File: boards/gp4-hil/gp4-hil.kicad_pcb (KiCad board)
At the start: 4 copper layers, 160 x 62 mm, 452 parts, among them J1 BEL_FUSE_0826-1G1T-23-F, J2 XILINX_JTAG, J3 XILINX_JTAG_ICESIDE, J4 XILINX_JTAG_ICESIDE, K1 CONN_3_PWROUT, P1 GPAK_ZIF, P2 2x10 HEADER, Q1 SSM6N58NU, Q11 SSM6N58NU, Q12 DMP2069UFY4, Q13 SSM6N58NU, Q14 SSM6N58NU, Q15 SSM6N58NU, Q16 SSM6N58NU, Q17 SSM6N58NU, Q18 SSM6N58NU, Q19 SSM6N58NU, Q20 SSM6N58NU, Q21 SSM6N58NU, Q22 DMP2069UFY4, U1 MIC2288-DFN, U10 AD9609, U11 DAC084S085, U12 DAC084S085, U13 DAC084S085, U14 DAC084S085, U15 TS3A4751, U16 TS3A4751, U17 TS3A4751, U18 TS3A4751, U19 TS3A4751, U2 XC7A100T-1FTG256C, U20 SIP32408, U21 SIP32408, U22 SIP32408, U23 SIP32408, U24 SIP32408, U25 TS3A4751, U26 TS3A4751, U27 TS3A4751, U28 TS3A4751, U29 TXB0104RUT, U3 LTC3374-QFN, U30 TXB0104RUT, U31 ADA4937-2, U32 SIP32408, U33 125 MHz, U34 INA199A2RSW, U35 INA199A2RSW, U36 INA199A2RSW, U4 SIP32408, U5 KSZ9031RN, U6 W25Q32FW, U7 25 MHz, U8 ADG726, U9 AD9609

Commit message: Continued work on GreenPak test board
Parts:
- C146, C148, C150, C153, C154, C185, C42, C43, C44, C45, R139, R141, R17, R22: moved to B.Cu
- moved C154 101.3 mm to (123.0, 70.6), turned to 180 degrees
- moved C152 96.3 mm to (116.7, 83.5), turned to 90 degrees
- moved R141 93.9 mm to (124.7, 71.0), turned to 90 degrees
- moved R74 89.9 mm to (127.5, 77.4), turned to 180 degrees
- moved R140 88.3 mm to (116.2, 85.0)
- moved C159 86.5 mm to (60.2, 51.5)
- moved C160 86.5 mm to (63.4, 48.5)
- moved C161 86.5 mm to (60.0, 48.5)
- moved C162 86.5 mm to (63.5, 51.3)
- moved U19 86.5 mm to (56.3, 50.9)
- moved U25 86.5 mm to (46.2, 50.5)
- moved U26 86.5 mm to (51.6, 51.1)
- moved U27 86.5 mm to (41.2, 50.6)
- moved U28 86.5 mm to (35.8, 51.0)
- moved C153 85.3 mm to (123.0, 71.4), turned to 180 degrees
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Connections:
- C151 pad 1: Net-(C151-Pad1) -> /Analog IO/ADC_B_CLKX_P
- C152 pad 1: Net-(C152-Pad1) -> /Analog IO/ADC_B_CLKX_N
- C153 pad 1: Net-(C153-Pad1) -> /Analog IO/ADC_A_CLKX_P
- C154 pad 1: Net-(C154-Pad1) -> /Analog IO/ADC_A_CLKX_N
- R140 pad 1: Net-(C151-Pad1) -> /Analog IO/ADC_B_CLKX_P
- R140 pad 2: Net-(C152-Pad1) -> /Analog IO/ADC_B_CLKX_N
- R141 pad 1: Net-(C153-Pad1) -> /Analog IO/ADC_A_CLKX_P
- R141 pad 2: Net-(C154-Pad1) -> /Analog IO/ADC_A_CLKX_N
- U2 pad A12: /Analog IO/ADC_B_D2 -> /Analog IO/ADC_B_MODE
- U2 pad A13: Net-(C151-Pad1) -> /Analog IO/ADC_SCLK
- U2 pad A14: Net-(C152-Pad1) -> /Analog IO/ADC_B_SDIO
- U2 pad A15: /Analog IO/ADC_CS_N -> /Analog IO/ADC_B_D5
- U2 pad A8: /Analog IO/MUX_A3 -> /Analog IO/ADC_B_CLKX_P
- U2 pad A9: /Analog IO/MUX_CS_A_N -> /Analog IO/ADC_B_CLKX_N
- U2 pad B11: /Analog IO/ADC_B_D0 -> /Analog IO/MUX_A3
- U2 pad B12: /Analog IO/ADC_B_D1 -> /Analog IO/ADC_CS_N
- U2 pad B14: /Analog IO/ADC_B_D8 -> /Analog IO/ADC_B_D6
- U2 pad B15: /Analog IO/ADC_B_D9 -> /Analog IO/ADC_B_D2
- U2 pad B16: Net-(C154-Pad1) -> /Analog IO/ADC_B_D4
- U2 pad C11: /Analog IO/ADC_SCLK -> /Analog IO/DAC_SYNC_N
- U2 pad C12: /Analog IO/ADC_B_SDIO -> /Analog IO/ADC_A_MODE
- U2 pad C13: (no net) -> /Analog IO/ADC_A_SDIO
- U2 pad C14: /Analog IO/ADC_B_D7 -> /Analog IO/ADC_B_D8
- U2 pad C16: Net-(C153-Pad1) -> /Analog IO/ADC_B_D3
- U2 pad D14: /Analog IO/DAC_SCLK -> /Analog IO/ADC_A_CLKX_P
- U2 pad D15: /Analog IO/DAC_SYNC_N -> /Analog IO/ADC_A_CLKX_N
- U2 pad D16: /Analog IO/ADC_B_D6 -> /Analog IO/ADC_B_D1
- U2 pad D8: /Analog IO/ADC_B_D3 -> /Analog IO/DAC_SCLK
- U2 pad D9: /Analog IO/ADC_B_D4 -> /Analog IO/DAC_C_DIN
- U2 pad E15: /Analog IO/ADC_B_D5 -> /Analog IO/ADC_B_D0
- U2 pad F13: /Analog IO/ADC_B_MODE -> /Analog IO/ADC_B_D9
- U2 pad G11: /Analog IO/ADC_A_MODE -> /Analog IO/MUX_CS_A_N
- U2 pad G12: /Analog IO/ADC_A_D8 -> /Analog IO/ADC_B_D7
- U2 pad H11: /Analog IO/DAC_C_DIN -> (no net)
- U2 pad H12: /Analog IO/ADC_A_SDIO -> /Analog IO/ADC_A_D8
- U8 pad 30: /Analog IO/ADC_GPIO20 -> /Analog IO/ADC_VDD2
- U8 pad 32: /Analog IO/ADC_VDD2 -> /Analog IO/ADC_GPIO20
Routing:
- net /Analog IO/A1V8: track 17.3 -> 102.0 mm, vias 5 -> 13
- net /Analog IO/GND: track 1086.6 -> 1147.2 mm, vias 210 -> 222
- net /Analog IO/ADC_GPIO20: track 0.00 -> 54.0 mm, vias 0 -> 1
- net /Analog IO/ADC_A_MODE: track 2.04 -> 37.8 mm, vias 1 -> 4
- net /Analog IO/ADC_A_CLKX_P: track 0.00 -> 35.0 mm, vias 0 -> 1
- net /Analog IO/ADC_A_CLKX_N: track 0.00 -> 34.9 mm, vias 0 -> 1
- net /Analog IO/ADC_A_DCLK: track 9.65 -> 42.7 mm
- net /Analog IO/ADC_CS_N: track 0.00 -> 31.1 mm, vias 0 -> 2
- net /Analog IO/ADC_B_D7: track 0.71 -> 31.3 mm, vias 1 -> 2
- net /Analog IO/ADC_A_SDIO: track 0.71 -> 31.2 mm, vias 1 -> 4
- net /Analog IO/ADC_SCLK: track 0.71 -> 28.9 mm, vias 1 -> 2
- net /Analog IO/ADC_B_D6: track 0.00 -> 27.2 mm, vias 0 -> 2
- net /Analog IO/ADC_B_D9: track 0.00 -> 26.8 mm, vias 0 -> 2
- net /Analog IO/ADC_B_D8: track 0.00 -> 25.7 mm, vias 0 -> 2
- net /Analog IO/ADC_B_D5: track 0.71 -> 25.8 mm, vias 1 -> 2
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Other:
- rule via_min_size: 0.55 -> 0.5
- board text added: "GreenPak Toolchain Test v0.1 A. Zonenberg / 2016-06-07"
- board text removed: "GreenPak Toolchain Test v0.1 A. Zonenberg / 2016-06-03"

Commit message: Added logic to check if the node displaced by a swap is legal in the current site. Fixes #9.
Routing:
- net /FPGA support/1V0: track 130.4 -> 132.2 mm
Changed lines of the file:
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@@
     (thickness 1.6)
     (drawings 64)
-    (tracks 5589)
+    (tracks 5595)
     (zones 0)
     (modules 452)
@@
   (segment (start 108 91) (end 107.5 90.5) (width 0.15) (layer F.Cu) (net 14) (status 10))
   (via (at 107.5 90.5) (size 0.55) (drill 0.3) (layers F.Cu B.Cu) (net 14))
+  (segment (start 112.900001 82.374999) (end 120.65 82.374999) (width 0.15) (layer In2.Cu) (net 15))
+  (segment (start 121.082008 79.117992) (end 120.553092 79.646908) (width 0.15) (layer In2.Cu) (net 15))
+  (segment (start 120.553092 79.646908) (end 120.553092 80.56417) (width 0.15) (layer In2.Cu) (net 15))
+  (segment (start 120.775001 82.249998) (end 120.65 82.374999) (width 0.15) (layer In2.Cu) (net 15))
+  (segment (start 120.553092 80.56417) (end 120.775001 80.786079) (width 0.15) (layer In2.Cu) (net 15))
+  (segment (start 120.775001 80.786079) (end 120.775001 82.249998) (width 0.15) (layer In2.Cu) (net 15))
+  (segment (start 124.05 79.117992) (end 126.374999 76.792993) (width 0.15) (layer In2.Cu) (net 15))
+  (segment (start 124.05 79.117992) (end 121.082008 79.117992) (width 0.15) (layer In2.Cu) (net 15))
   (segment (start 112.475 82.8) (end 112.475 77.25) (width 0.15) (layer In2.Cu) (net 15))
+  (segment (start 112.525 77.3) (end 112.475 77.25) (width 0.15) (layer In2.Cu) (net 15))
+  (segment (start 113.5 77.3) (end 112.525 77.3) (width 0.15) (layer In2.Cu) (net 15))
   (segment (start 112.475 83.75) (end 112.475 82.8) (width 0.15) (layer In2.Cu) (net 15))
   (segment (start 126.374999 75.225001) (end 126.85 74.75) (width 0.15) (layer In2.Cu) (net 15))
   (segment (start 126.85 74.75) (end 132.303002 74.75) (width 0.15) (layer In2.Cu) (net 15))
   (segment (start 112.475 82.8) (end 112.900001 82.374999) (width 0.15) (layer In2.Cu) (net 15))
-  (segment (start 112.900001 82.374999) (end 120.792993 82.374999) (width 0.15) (layer In2.Cu) (net 15))
-  (segment (start 120.792993 82.374999) (end 126.374999 76.792993) (width 0.15) (layer In2.Cu) (net 15))
   (segment (start 126.374999 76.792993) (end 126.374999 75.225001) (width 0.15) (layer In2.Cu) (net 15))
   (segment (start 115.2 78.05) (end 113.5 78.05) (width 0.15) (layer In2.Cu) (net 15))
@@
   (segment (start 113.48507 78.78507) (end 113.5 78.8) (width 0.15) (layer F.Cu) (net 15))
   (via (at 113.5 78.8) (size 0.55) (drill 0.3) (layers F.Cu B.Cu) (net 15))
-  (segment (start 113.5 77.3) (end 112.525 77.3) (width 0.15) (layer In2.Cu) (net 15))
-  (segment (start 112.525 77.3) (end 112.475 77.25) (width 0.15) (layer In2.Cu) (net 15))
   (segment (start 113.48507 78.05) (end 113.48507 77.31493) (width 0.15) (layer F.Cu) (net 15))
   (segment (start 113.48507 77.31493) (end 113.5 77.3) (width 0.15) (layer F.Cu) (net 15))

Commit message: Pushing current state of greenpak test board
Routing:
- net /FPGA support/1V0: track 132.2 -> 126.4 mm
- net /Analog IO/2V5: track 224.2 -> 228.3 mm, vias 23 -> 25
- added copper zone on F.Cu, net /Analog IO/2V5
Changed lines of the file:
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@@
   (general
     (links 1341)
-    (no_connects 444)
+    (no_connects 443)
     (area 15.966071 41.4125 184.744643 140.2125)
     (thickness 1.6)
     (drawings 64)
-    (tracks 5595)
+    (tracks 5600)
     (zones 0)
     (modules 452)
@@
   (via (at 150.4 72.3) (size 0.55) (drill 0.3) (layers F.Cu B.Cu) (net 2))
   (via (at 150.4 71.3) (size 0.55) (drill 0.3) (layers F.Cu B.Cu) (net 2))
+  (segment (start 125.1 67.4) (end 125.1 66.15) (width 0.15) (layer In2.Cu) (net 3))
+  (segment (start 125.1 66.15) (end 124.6 65.65) (width 0.15) (layer In2.Cu) (net 3))
+  (segment (start 125.1 67.4) (end 124.25 67.4) (width 0.15) (layer In2.Cu) (net 3))
+  (segment (start 124.65 68.188908) (end 124.65 67.85) (width 0.15) (layer F.Cu) (net 3))
+  (segment (start 124.65 67.85) (end 125.1 67.4) (width 0.15) (layer F.Cu) (net 3))
+  (via (at 125.1 67.4) (size 0.55) (drill 0.3) (layers F.Cu B.Cu) (net 3))
+  (segment (start 124.078859 78.386131) (end 124.078859 74.971141) (width 0.15) (layer B.Cu) (net 3))
+  (segment (start 124.078859 74.971141) (end 124.1 74.95) (width 0.15) (layer B.Cu) (net 3))
+  (segment (start 124.65 68.188908) (end 124.65 74.4) (width 0.15) (layer F.Cu) (net 3))
+  (segment (start 124.65 74.4) (end 124.1 74.95) (width 0.15) (layer F.Cu) (net 3))
+  (via (at 124.1 74.95) (size 0.55) (drill 0.3) (layers F.Cu B.Cu) (net 3))
+  (segment (start 124.25 67.4) (end 124.25 67.788908) (width 0.15) (layer F.Cu) (net 3))
+  (segment (start 124.25 67.788908) (end 124.65 68.188908) (width 0.15) (layer F.Cu) (net 3))
   (segment (start 121.525 90.1) (end 121.525 89.525) (width 0.15) (layer B.Cu) (net 3))
   (segment (start 121.525 89.525) (end 121.5 89.5) (width 0.15) (layer B.Cu) (net 3))
@@
   (segment (start 119.975001 92.225001) (end 120 92.25) (width 0.125) (layer In2.Cu) (net 3))
   (segment (start 120 92.25) (end 120 93.5) (width 0.125) (layer In2.Cu) (net 3))
-  (segment (start 124.078859 78.386131) (end 124.078859 67.571141) (width 0.15) (layer In2.Cu) (net 3))
-  (segment (start 124.078859 67.571141) (end 124.25 67.4) (width 0.15) (layer In2.Cu) (net 3))
   (segment (start 142.25 78.5) (end 129.75 78.5) (width 0.15) (layer In2.Cu) (net 3))
   (segment (start 129.75 78.5) (end 121.5 86.75) (width 0.15) (layer In2.Cu) (net 3))
@@
   (segment (start 155.22 91.405) (end 155.22 90.22) (width 0.15) (layer B.Cu) (net 10) (status 30))
   (segment (start 155.22 90.22) (end 155.2 90.2) (width 0.15) (layer B.Cu) (net 10) (status 30))
-  (segment (start 120.524999 69.971999) (end 119.1 71.396998) (width 0.15) (layer In2.Cu) (net 11))
-  (segment (start 119.1 71.396998) (end 119.128687 71.425685) (width 0.15) (layer In2.Cu) (net 11))
-  (segment (start 119.128687 71.425685) (end 119.128687 75.462845) (width 0.15) (layer In2.Cu) (net 11))
-  (segment (start 120.25 68.95) (end 120.524999 69.224999) (width 0.15) (layer In2.Cu) (net 11))
-  (segment (start 120.524999 69.224999) (end 120.524999 69.971999) (width 0.15) (layer In2.Cu) (net 11))
+  (segment (start 119.128687 75.462845) (end 119.128687 71.368311) (width 0.15) (layer In2.Cu) (net 11))
+  (segment (start 119.128687 71.368311) (end 120.524999 69.971999) (width 0.15) (layer In2.Cu) (net 11))
+  (segment (start 120.524999 69.971999) (end 120.524999 69.224999) (width 0.15) (layer In2.Cu) (net 11))
+  (segment (start 120.524999 69.224999) (end 120.25 68.95) (width 0.15) (layer In2.Cu) (net 11))
   (segment (start 87.174999 65.975001) (end 92.125001 61.024999) (width 0.15) (layer In2.Cu) (net 11))
   (segment (start 118.746998 62.8) (end 118.861092 62.8) (width 0.15) (layer In2.Cu) (net 11))
@@
   (segment (start 108 91) (end 107.5 90.5) (width 0.15) (layer F.Cu) (net 14) (status 10))
   (via (at 107.5 90.5) (size 0.55) (drill 0.3) (layers F.Cu B.Cu) (net 14))
-  (segment (start 112.900001 82.374999) (end 120.65 82.374999) (width 0.15) (layer In2.Cu) (net 15))
-  (segment (start 121.082008 79.117992) (end 120.553092 79.646908) (width 0.15) (layer In2.Cu) (net 15))
-  (segment (start 120.553092 79.646908) (end 120.553092 80.56417) (width 0.15) (layer In2.Cu) (net 15))
-  (segment (start 120.775001 82.249998) (end 120.65 82.374999) (width 0.15) (layer In2.Cu) (net 15))
-  (segment (start 120.553092 80.56417) (end 120.775001 80.786079) (width 0.15) (layer In2.Cu) (net 15))
-  (segment (start 120.775001 80.786079) (end 120.775001 82.249998) (width 0.15) (layer In2.Cu) (net 15))
-  (segment (start 124.05 79.117992) (end 126.374999 76.792993) (width 0.15) (layer In2.Cu) (net 15))
-  (segment (start 124.05 79.117992) (end 121.082008 79.117992) (width 0.15) (layer In2.Cu) (net 15))
-  (segment (start 112.475 82.8) (end 112.475 77.25) (width 0.15) (layer In2.Cu) (net 15))
-  (segment (start 112.525 77.3) (end 112.475 77.25) (width 0.15) (layer In2.Cu) (net 15))
-  (segment (start 113.5 77.3) (end 112.525 77.3) (width 0.15) (layer In2.Cu) (net 15))
-  (segment (start 112.475 83.75) (end 112.475 82.8) (width 0.15) (layer In2.Cu) (net 15))
-  (segment (start 126.374999 75.225001) (end 126.85 74.75) (width 0.15) (layer In2.Cu) (net 15))
-  (segment (start 126.85 74.75) (end 132.303002 74.75) (width 0.15) (layer In2.Cu) (net 15))
-  (segment (start 112.475 82.8) (end 112.900001 82.374999) (width 0.15) (layer In2.Cu) (net 15))
-  (segment (start 126.374999 76.792993) (end 126.374999 75.225001) (width 0.15) (layer In2.Cu) (net 15))
+  (segment (start 113.5 77.3) (end 112.725 77.3) (width 0.15) (layer In2.Cu) (net 15))
+  (segment (start 112.725 77.3) (end 112.475 77.55) (width 0.15) (layer In2.Cu) (net 15))
+  (segment (start 112.475 77.55) (end 112.475 83.75) (width 0.15) (layer In2.Cu) (net 15))
+  (segment (start 112.475 83.75) (end 112.95 84.225) (width 0.15) (layer In2.Cu) (net 15))
+  (segment (start 120.4 76.1) (end 114.7 76.1) (width 0.15) (layer In2.Cu) (net 15))
+  (segment (start 114.7 76.1) (end 113.5 77.3) (width 0.15) (layer In2.Cu) (net 15))
+  (segment (start 122.15 74.35) (end 120.4 76.1) (width 0.15) (layer In2.Cu) (net 15))
+  (segment (start 125.85 74.35) (end 122.15 74.35) (width 0.15) (layer In2.Cu) (net 15))
+  (segment (start 126.25 74.75) (end 125.85 74.35) (width 0.15) (layer In2.Cu) (net 15))
+  (segment (start 126.95 74.75) (end 132.303002 74.75) (width 0.15) (layer In2.Cu) (net 15))
+  (segment (start 126.85 74.75) (end 126.95 74.75) (width 0.15) (layer In2.Cu) (net 15))
+  (segment (start 126.95 74.75) (end 126.25 74.75) (width 0.15) (layer In2.Cu) (net 15))
   (segment (start 115.2 78.05) (end 113.5 78.05) (width 0.15) (layer In2.Cu) (net 15))
   (segment (start 113.48507 78.05) (end 115.2 78.05) (width 0.15) (layer F.Cu) (net 15))
@@
   (segment (start 112.65 84.2) (end 112.65 83.5) (width 0.15) (layer B.Cu) (net 15))
   (segment (start 112.65 83.5) (end 112.7 83.45) (width 0.15) (layer B.Cu) (net 15))
-  (segment (start 112.95 84.225) (end 112.475 83.75) (width 0.15) (layer In2.Cu) (net 15))
   (segment (start 113.45 84.725) (end 112.95 84.225) (width 0.15) (layer In2.Cu) (net 15))
   (segment (start 112.95 84.225) (end 112.675 84.225) (width 0.15) (layer In2.Cu) (net 15))
@@
       (pts
         (xy 157.5 75.5) (xy 166 75.5) (xy 166 65.5) (xy 140.5 65.5) (xy 140.5 75.5)
-        (xy 115 75.5) (xy 115 92.75) (xy 117 92.75) (xy 117 95) (xy 116 95)
-        (xy 116 98.5) (xy 121.75 98.5) (xy 121.75 79.5) (xy 158.5 79.5) (xy 158.5 86.25)
-        (xy 149.75 86.25) (xy 149.75 87.25) (xy 149 87.25) (xy 149 100.25) (xy 144 100.25)
-        (xy 144 106.5) (xy 151.75 106.5) (xy 151.75 88.25) (xy 179.75 88.25) (xy 179.75 82.5)
-        (xy 165 82.75) (xy 165 77.75) (xy 143.75 77.75) (xy 143.75 66.75) (xy 157.5 66.75)
+        (xy 122.25 75.5) (xy 122.25 76.75) (xy 115 76.75) (xy 115 92.75) (xy 117 92.75)
+        (xy 117 95) (xy 116 95) (xy 116 98.5) (xy 121.75 98.5) (xy 121.75 79.5)
+        (xy 158.5 79.5) (xy 158.5 86.25) (xy 149.75 86.25) (xy 149.75 87.25) (xy 149 87.25)
+        (xy 149 100.25) (xy 144 100.25) (xy 144 106.5) (xy 151.75 106.5) (xy 151.75 88.25)
+        (xy 179.75 88.25) (xy 179.75 82.5) (xy 165 82.75) (xy 165 77.75) (xy 143.75 77.75)
+        (xy 143.75 66.75) (xy 157.5 66.75)
       )
     )
@@
     (polygon
       (pts
-        (xy 140.25 65.5) (xy 140.25 75.25) (xy 114.75 75.25) (xy 114.75 93) (xy 116.75 93)
-        (xy 116.75 94.75) (xy 115.75 94.75) (xy 115.75 96) (xy 114.75 96) (xy 114.75 101)
-        (xy 110.75 101) (xy 110.75 94.5) (xy 112 94.5) (xy 112 97.75) (xy 112.75 97.75)
-        (xy 112.75 93) (xy 112 93) (xy 112 65.5)
+        (xy 140.25 69.75) (xy 140.25 75.25) (xy 121.75 75.25) (xy 121.75 76.5) (xy 114.75 76.5)
+        (xy 114.75 93) (xy 116.75 93) (xy 116.75 94.75) (xy 115.75 94.75) (xy 115.75 96)
+        (xy 114.75 96) (xy 114.75 101) (xy 110.75 101) (xy 110.75 94.5) (xy 112 94.5)
+        (xy 112 97.75) (xy 112.75 97.75) (xy 112.75 93) (xy 112 93) (xy 112 69.75)
+      )
+    )
+  )
+  (zone (net 3) (net_name "/Analog IO/2V5") (layer F.Cu) (hatch edge 0.508)
+    (connect_pads (clearance 0.15))
+    (min_thickness 0.15)
+    (fill yes (arc_segments 16) (thermal_gap 0.25) (thermal_bridge_width 0.2))
+    (polygon
+      (pts
+        (xy 123.95 67.05) (xy 123.95 75.6) (xy 125.5 75.6) (xy 125.5 69.35) (xy 125.5 67.05)
       )
     )

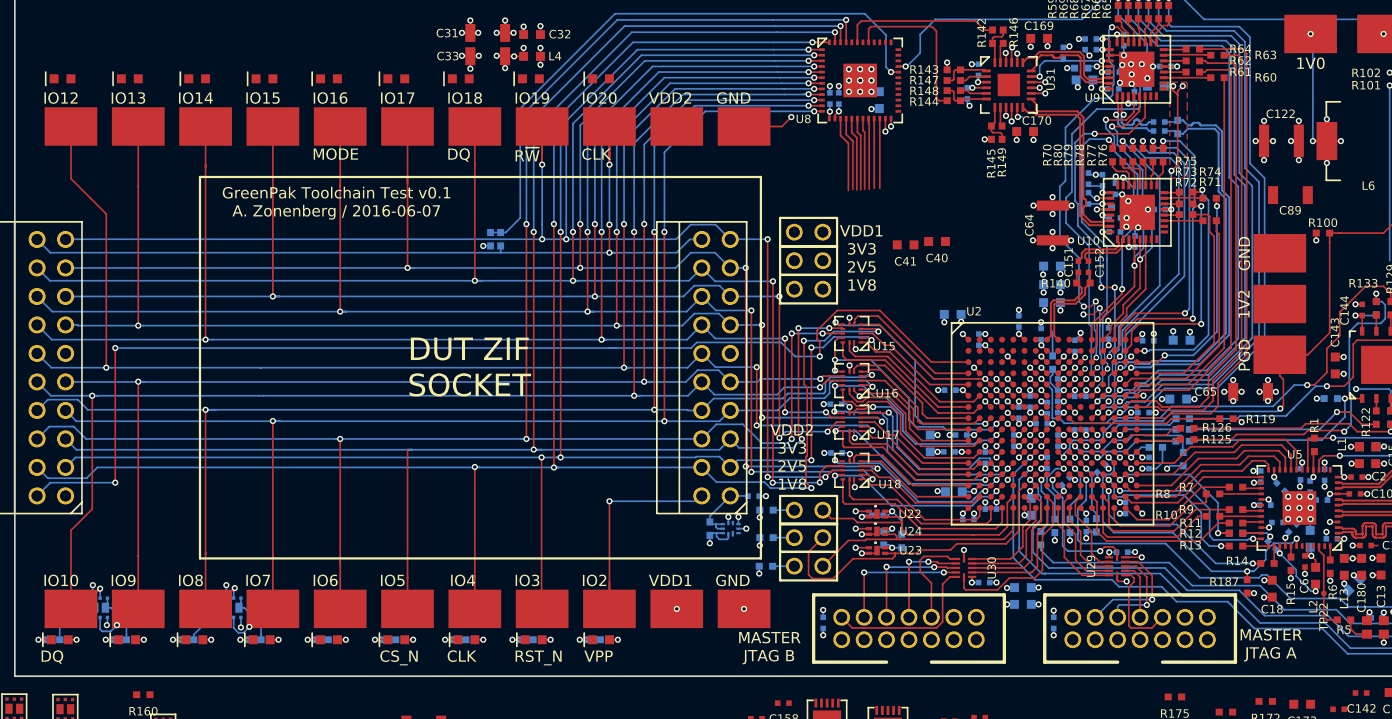
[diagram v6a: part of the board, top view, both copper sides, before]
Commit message: Major cleanup of power routing on test board. Less than 400 unrouted nets, but still lots more to do.
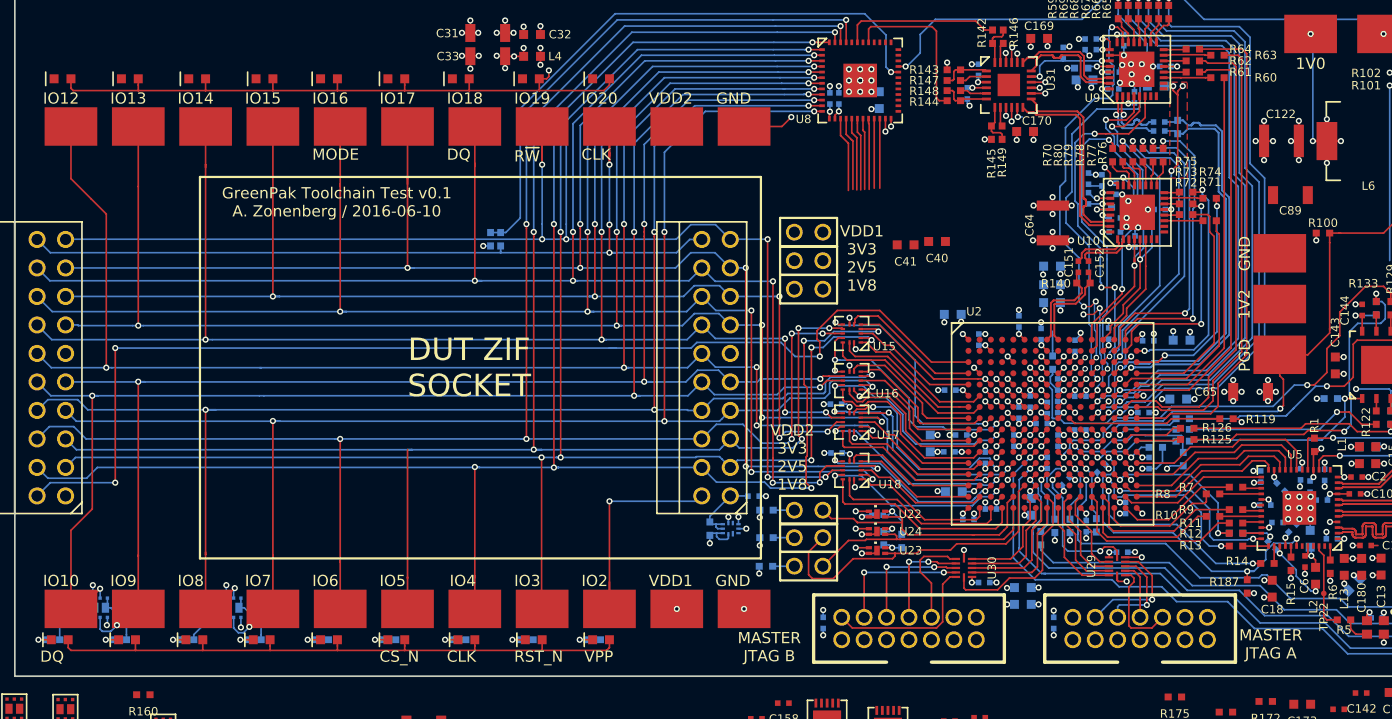
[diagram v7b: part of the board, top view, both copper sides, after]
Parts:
- moved C42 0.05 mm to (119.2, 76.5)
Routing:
- net /Analog IO/1V8: track 315.1 -> 474.4 mm, vias 55 -> 56
- net /Analog IO/3V3: track 122.8 -> 239.8 mm, vias 17 -> 9
- net /Analog IO/2V5: track 228.3 -> 244.9 mm
- net /Analog IO/DUT_VDD1: track 140.6 -> 149.5 mm
- net /Analog IO/A1V8: track 102.0 -> 109.7 mm, vias 13 -> 14
- net /Ethernet + JTAG/1V2: track 69.4 -> 68.7 mm
- net /Analog IO/DUT_VDD2: track 29.4 -> 29.9 mm
- added copper zone on In2.Cu, net /Analog IO/3V3
- added copper zone on In2.Cu, net /Analog IO/A1V8
- added copper zone on In2.Cu, net /Analog IO/A3V3
- added copper zone on In2.Cu, net /Analog IO/DUT_VDD1
- added copper zone on In2.Cu, net /Analog IO/DUT_VDD2
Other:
- board text added: "GreenPak Toolchain Test v0.1 A. Zonenberg / 2016-06-10"
- board text removed: "GreenPak Toolchain Test v0.1 A. Zonenberg / 2016-06-07"
